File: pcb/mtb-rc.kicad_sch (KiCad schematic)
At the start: 44 parts, among them J1 MVE252-5-V, J10 MVE252-5-V, J11 MVE252-5-V, J2 MVE252-5-V, J3 MVE252-5-V, J4 MVE252-5-V, J5 MVE252-5-V, J9 MVE252-5-V, U1 VO0631T, U2 VO0631T, U3 VO0631T

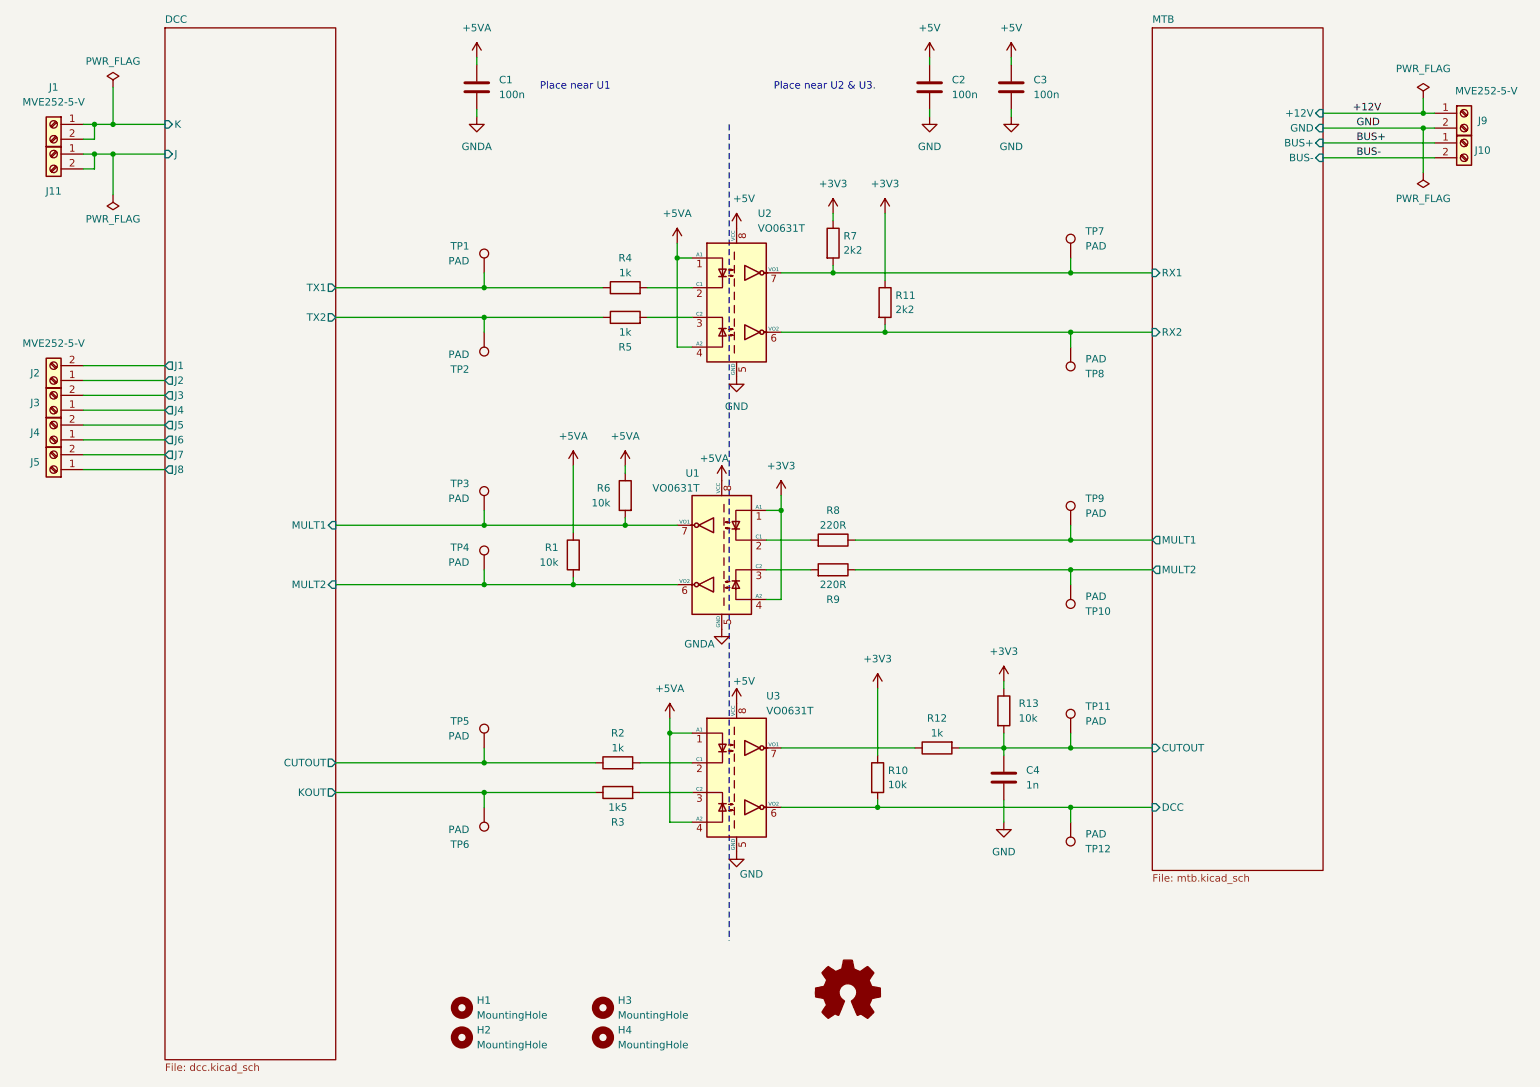
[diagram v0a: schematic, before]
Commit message: Use 2×MVE252-5-V footprint.
To avoid DRC issues in PCB.
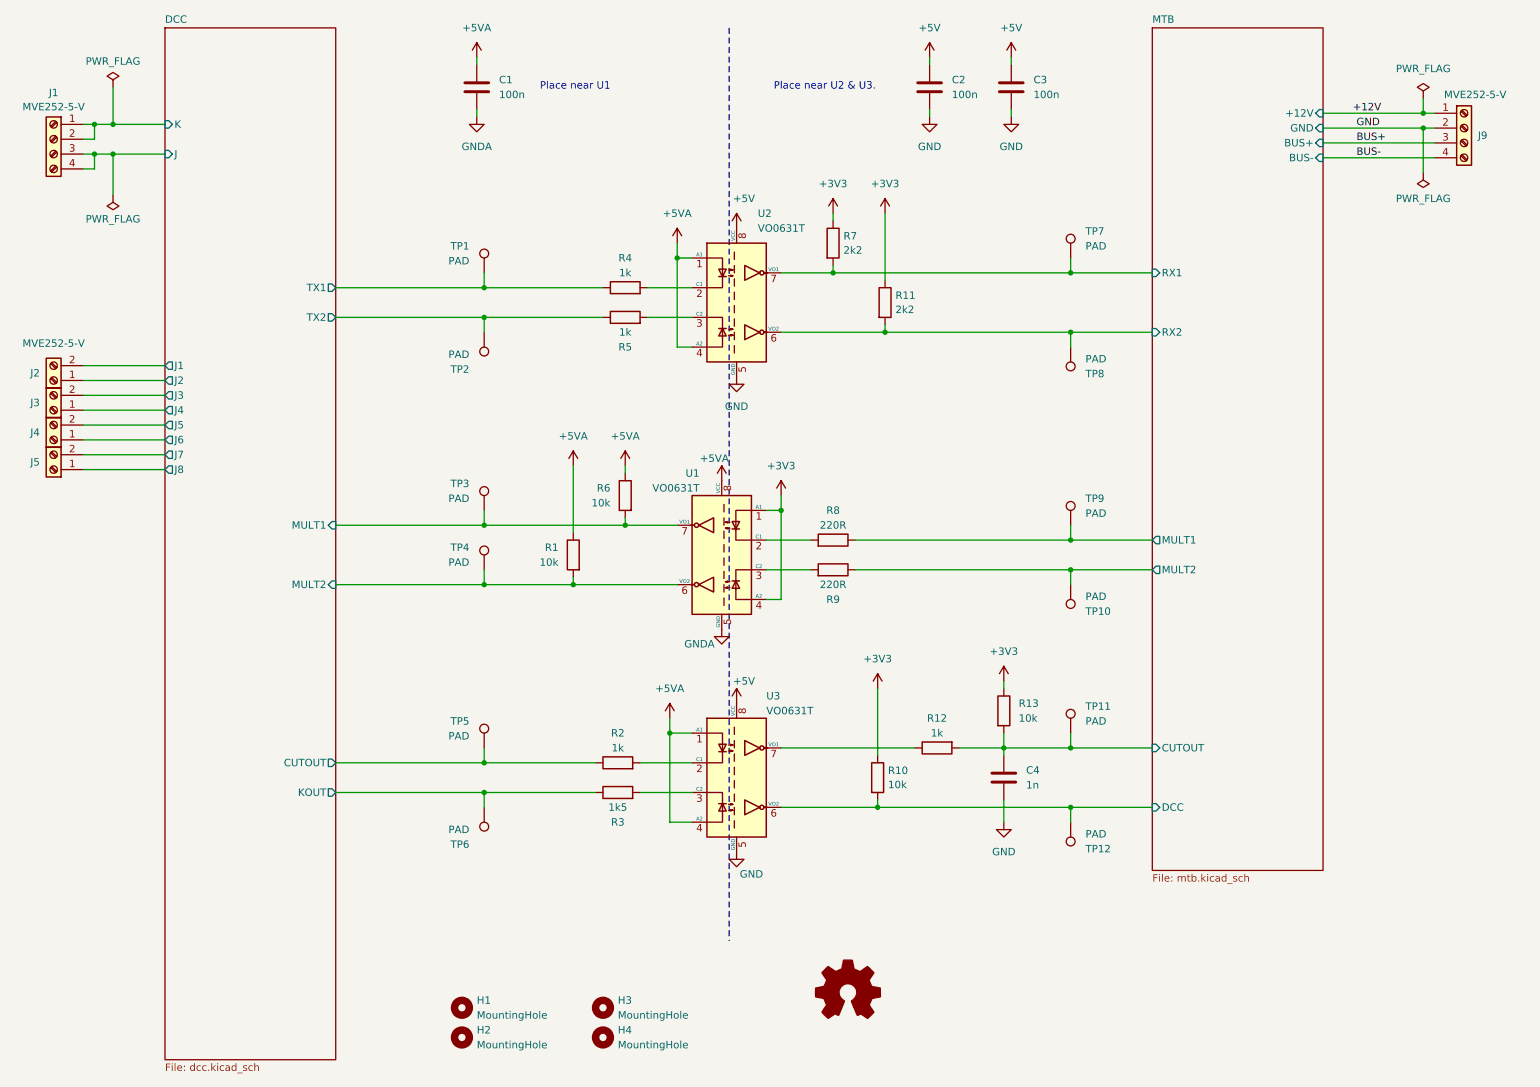
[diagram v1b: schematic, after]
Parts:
- removed J10, J11: MVE252-5-V, TerminalBlock_Euroclamp:MVE252-5-V, symbol Connector:Screw_Terminal_01x02
- J1, J9: footprint TerminalBlock_Euroclamp:MVE252-5-V -> TerminalBlock_Euroclamp:MVE252-5-V-2x; symbol Connector:Screw_Terminal_01x02 -> Connector:Screw_Terminal_01x04
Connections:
- net BUS+: now also J9.3 (Pin_3)
- net BUS-: now also J9.4 (Pin_4)
- net DCC/J: now also J1.3 (Pin_3), J1.4 (Pin_4)
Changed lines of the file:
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@@
     (stroke (width 0) (type default))
   )
-  (polyline (pts (xy 144.78 33.02) (xy 144.78 172.72))
+  (polyline (pts (xy 144.78 16.51) (xy 144.78 172.72))
     (stroke (width 0) (type dash))
   )
@@
     )
   )
-  (symbol (lib_id "Connector:Screw_Terminal_01x02") (at 29.21 33.02 0) (mirror y) (unit 1)
-    (in_bom yes) (on_board yes) (dnp no) (fields_autoplaced)
-    (property "Reference" "J1" (at 29.21 26.67 0)
-      (effects (font (size 1.27 1.27)))
-    )
-    (property "Value" "MVE252-5-V" (at 29.21 29.21 0)
-      (effects (font (size 1.27 1.27)))
-    )
-    (property "Footprint" "TerminalBlock_Euroclamp:MVE252-5-V" (at 29.21 33.02 0)
-      (effects (font (size 1.27 1.27)) hide)
-    )
-    (property "Datasheet" "~" (at 29.21 33.02 0)
-      (effects (font (size 1.27 1.27)) hide)
-    )
-    (pin "1")
-    (pin "2")
+  (symbol (lib_id "Connector:Screw_Terminal_01x04") (at 29.21 35.56 0) (mirror y) (unit 1)
+    (in_bom yes) (on_board yes) (dnp no) (fields_autoplaced)
+    (property "Reference" "J1" (at 29.21 27.6057 0)
+      (effects (font (size 1.27 1.27)))
+    )
+    (property "Value" "MVE252-5-V" (at 29.21 30.0299 0)
+      (effects (font (size 1.27 1.27)))
+    )
+    (property "Footprint" "TerminalBlock_Euroclamp:MVE252-5-V-2x" (at 29.21 35.56 0)
+      (effects (font (size 1.27 1.27)) hide)
+    )
+    (property "Datasheet" "~" (at 29.21 35.56 0)
+      (effects (font (size 1.27 1.27)) hide)
+    )
+    (pin "1")
+    (pin "2")
+    (pin "3")
+    (pin "4")
     (instances
       (project "mtb-rc"
@@
     )
   )
-  (symbol (lib_id "Connector:Screw_Terminal_01x02") (at 270.51 31.115 0) (unit 1)
-    (in_bom yes) (on_board yes) (dnp no)
-    (property "Reference" "J9" (at 273.685 32.385 0)
-      (effects (font (size 1.27 1.27)))
-    )
-    (property "Value" "MVE252-5-V" (at 274.32 27.305 0)
-      (effects (font (size 1.27 1.27)))
-    )
-    (property "Footprint" "TerminalBlock_Euroclamp:MVE252-5-V" (at 270.51 31.115 0)
-      (effects (font (size 1.27 1.27)) hide)
-    )
-    (property "Datasheet" "~" (at 270.51 31.115 0)
-      (effects (font (size 1.27 1.27)) hide)
-    )
-    (pin "1")
-    (pin "2")
+  (symbol (lib_id "Connector:Screw_Terminal_01x04") (at 270.51 33.655 0) (unit 1)
+    (in_bom yes) (on_board yes) (dnp no)
+    (property "Reference" "J9" (at 273.685 34.925 0)
+      (effects (font (size 1.27 1.27)))
+    )
+    (property "Value" "MVE252-5-V" (at 272.415 27.94 0)
+      (effects (font (size 1.27 1.27)))
+    )
+    (property "Footprint" "TerminalBlock_Euroclamp:MVE252-5-V-2x" (at 270.51 33.655 0)
+      (effects (font (size 1.27 1.27)) hide)
+    )
+    (property "Datasheet" "~" (at 270.51 33.655 0)
+      (effects (font (size 1.27 1.27)) hide)
+    )
+    (pin "1")
+    (pin "2")
+    (pin "3")
+    (pin "4")
     (instances
       (project "mtb-rc"
@@
         (path "/3e59d29f-2657-4552-9290-3c54fadfdf63"
           (reference "#FLG01") (unit 1)
-        )
-      )
-    )
-  )
-  (symbol (lib_id "Connector:Screw_Terminal_01x02") (at 29.21 38.1 0) (mirror y) (unit 1)
-    (in_bom yes) (on_board yes) (dnp no)
-    (property "Reference" "J11" (at 29.21 44.45 0)
-      (effects (font (size 1.27 1.27)))
-    )
-    (property "Value" "MVE252-5-V" (at 29.21 34.29 0)
-      (effects (font (size 1.27 1.27)) hide)
-    )
-    (property "Footprint" "TerminalBlock_Euroclamp:MVE252-5-V" (at 29.21 38.1 0)
-      (effects (font (size 1.27 1.27)) hide)
-    )
-    (property "Datasheet" "~" (at 29.21 38.1 0)
-      (effects (font (size 1.27 1.27)) hide)
-    )
-    (pin "1")
-    (pin "2")
-    (instances
-      (project "mtb-rc"
-        (path "/3e59d29f-2657-4552-9290-3c54fadfdf63"
-          (reference "J11") (unit 1)
         )
       )
@@
         )
       )
-    )
-  )
-  (symbol (lib_id "Connector:Screw_Terminal_01x02") (at 270.51 36.195 0) (unit 1)
-    (in_bom yes) (on_board yes) (dnp no)
-    (property "Reference" "J10" (at 273.685 37.465 0)
-      (effects (font (size 1.27 1.27)))
-    )
-    (property "Value" "MVE252-5-V" (at 270.51 32.385 0)
-      (effects (font (size 1.27 1.27)) hide)
-    )
-    (property "Footprint" "TerminalBlock_Euroclamp:MVE252-5-V" (at 270.51 36.195 0)
-      (effects (font (size 1.27 1.27)) hide)
-    )
-    (property "Datasheet" "~" (at 270.51 36.195 0)
-      (effects (font (size 1.27 1.27)) hide)
-    )
-    (pin "1")
-    (pin "2")
-    (instances
-      (project "mtb-rc"
-        (path "/3e59d29f-2657-4552-9290-3c54fadfdf63"
-          (reference "J10") (unit 1)
-        )
-      )

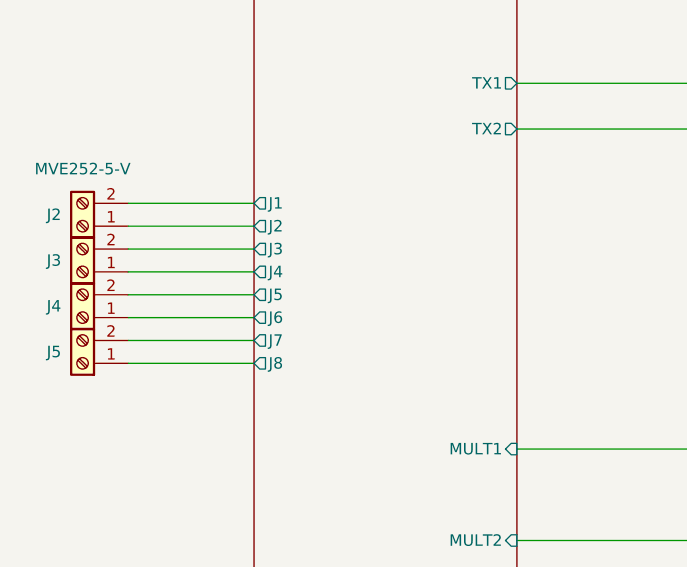
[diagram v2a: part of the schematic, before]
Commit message: J1-J8 -> J0-J7.
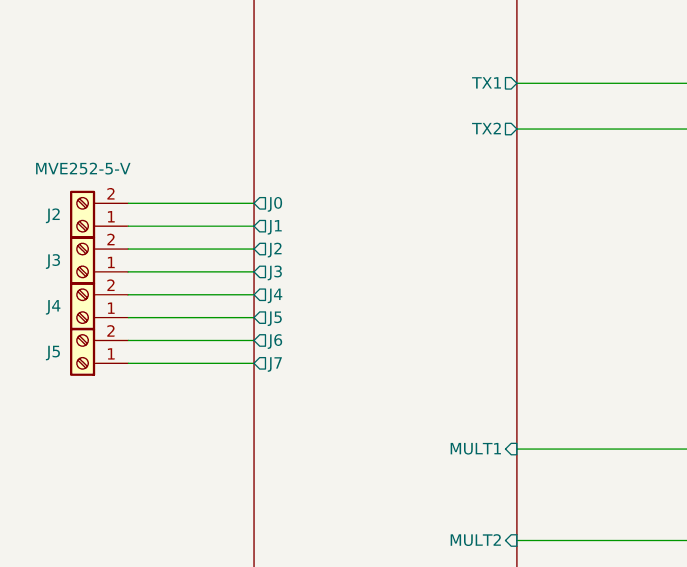
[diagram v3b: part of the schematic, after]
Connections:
- net DCC/J8 is gone; now on net DCC/J7: J5.1 (Pin_1)
- net DCC/J1: now also J2.1 (Pin_1); no longer J2.2 (Pin_2)
- net DCC/J2: now also J3.2 (Pin_2); no longer J2.1 (Pin_1)
- net DCC/J3: now also J3.1 (Pin_1); no longer J3.2 (Pin_2)
- net DCC/J4: now also J4.2 (Pin_2); no longer J3.1 (Pin_1)
- net DCC/J5: now also J4.1 (Pin_1); no longer J4.2 (Pin_2)
- net DCC/J6: now also J5.2 (Pin_2); no longer J4.1 (Pin_1)
- net DCC/J7: no longer J5.2 (Pin_2)
- new net DCC/J0: J2.2 (Pin_2)
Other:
- sheet DCC ports: added J0; removed J8
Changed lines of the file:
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@@
       (effects (font (size 1.27 1.27)) (justify left))
     )
-    (pin "J1" output (at 48.26 74.295 180)
+    (pin "J0" output (at 48.26 74.295 180)
       (effects (font (size 1.27 1.27)) (justify left))
     )
-    (pin "J2" output (at 48.26 76.835 180)
+    (pin "J1" output (at 48.26 76.835 180)
       (effects (font (size 1.27 1.27)) (justify left))
     )
-    (pin "J4" output (at 48.26 81.915 180)
+    (pin "J3" output (at 48.26 81.915 180)
       (effects (font (size 1.27 1.27)) (justify left))
     )
-    (pin "J3" output (at 48.26 79.375 180)
+    (pin "J2" output (at 48.26 79.375 180)
       (effects (font (size 1.27 1.27)) (justify left))
     )
-    (pin "J8" output (at 48.26 92.075 180)
+    (pin "J7" output (at 48.26 92.075 180)
       (effects (font (size 1.27 1.27)) (justify left))
     )
-    (pin "J7" output (at 48.26 89.535 180)
+    (pin "J6" output (at 48.26 89.535 180)
       (effects (font (size 1.27 1.27)) (justify left))
     )
@@
       (effects (font (size 1.27 1.27)) (justify right))
     )
-    (pin "J5" output (at 48.26 84.455 180)
+    (pin "J4" output (at 48.26 84.455 180)
       (effects (font (size 1.27 1.27)) (justify left))
     )
-    (pin "J6" output (at 48.26 86.995 180)
+    (pin "J5" output (at 48.26 86.995 180)
       (effects (font (size 1.27 1.27)) (justify left))
     )

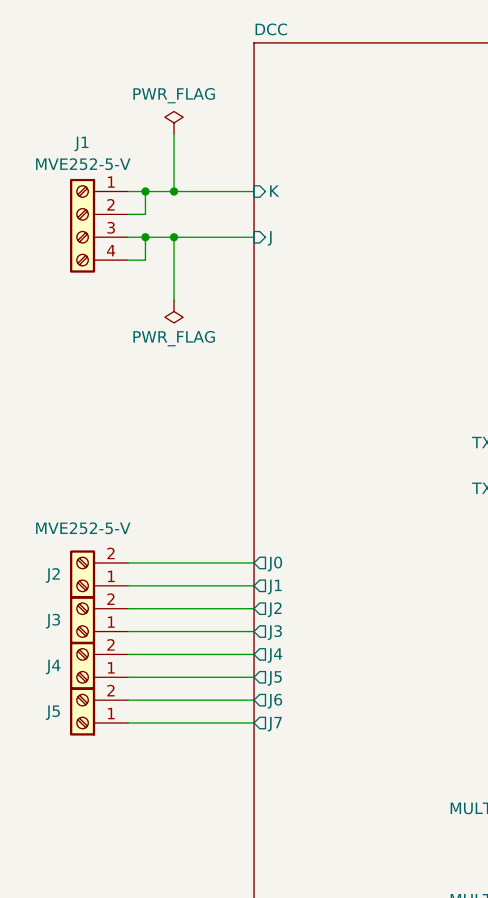
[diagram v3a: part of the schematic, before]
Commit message: Use 4×MVE252-5-V footprint.
To avoid DRC issues in schematics.
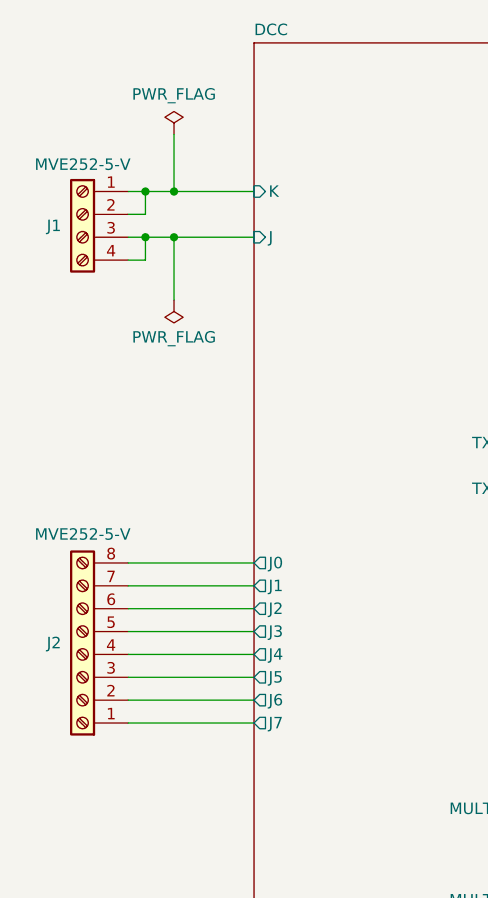
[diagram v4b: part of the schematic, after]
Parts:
- removed J3, J4, J5: MVE252-5-V, TerminalBlock_Euroclamp:MVE252-5-V, symbol Connector:Screw_Terminal_01x02
- J2: footprint TerminalBlock_Euroclamp:MVE252-5-V -> TerminalBlock_Euroclamp:MVE252-5-V-4x; symbol Connector:Screw_Terminal_01x02 -> Connector:Screw_Terminal_01x08
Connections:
- net DCC/J0: now also J2.8 (Pin_8); no longer J2.2 (Pin_2)
- net DCC/J1: now also J2.7 (Pin_7); no longer J2.1 (Pin_1)
- net DCC/J2: now also J2.6 (Pin_6)
- net DCC/J3: now also J2.5 (Pin_5)
- net DCC/J4: now also J2.4 (Pin_4)
- net DCC/J5: now also J2.3 (Pin_3)
- net DCC/J6: now also J2.2 (Pin_2)
- net DCC/J7: now also J2.1 (Pin_1)
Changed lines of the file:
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@@
-    )
-  )
-  (symbol (lib_id "Connector:Screw_Terminal_01x02") (at 29.21 86.995 180) (unit 1)
-    (in_bom yes) (on_board yes) (dnp no)
-    (property "Reference" "J4" (at 26.035 85.725 0)
-      (effects (font (size 1.27 1.27)))
-    )
-    (property "Value" "MVE252-5-V" (at 29.21 90.805 0)
-      (effects (font (size 1.27 1.27)) hide)
-    )
-    (property "Footprint" "TerminalBlock_Euroclamp:MVE252-5-V" (at 29.21 86.995 0)
-      (effects (font (size 1.27 1.27)) hide)
-    )
-    (property "Datasheet" "~" (at 29.21 86.995 0)
-      (effects (font (size 1.27 1.27)) hide)
-    )
-    (pin "1")
-    (pin "2")
-    (instances
-      (project "mtb-rc"
-        (path "/3e59d29f-2657-4552-9290-3c54fadfdf63"
-          (reference "J4") (unit 1)
-        )
-      )
     )
   )
@@
   )
   (symbol (lib_id "Connector:Screw_Terminal_01x04") (at 29.21 35.56 0) (mirror y) (unit 1)
-    (in_bom yes) (on_board yes) (dnp no) (fields_autoplaced)
-    (property "Reference" "J1" (at 29.21 27.6057 0)
+    (in_bom yes) (on_board yes) (dnp no)
+    (property "Reference" "J1" (at 26.035 36.83 0)
       (effects (font (size 1.27 1.27)))
     )
@@
         (path "/3e59d29f-2657-4552-9290-3c54fadfdf63"
           (reference "C1") (unit 1)
-        )
-      )
-    )
-  )
-  (symbol (lib_id "Connector:Screw_Terminal_01x02") (at 29.21 81.915 180) (unit 1)
-    (in_bom yes) (on_board yes) (dnp no)
-    (property "Reference" "J3" (at 26.035 80.645 0)
-      (effects (font (size 1.27 1.27)))
-    )
-    (property "Value" "MVE252-5-V" (at 29.21 85.725 0)
-      (effects (font (size 1.27 1.27)) hide)
-    )
-    (property "Footprint" "TerminalBlock_Euroclamp:MVE252-5-V" (at 29.21 81.915 0)
-      (effects (font (size 1.27 1.27)) hide)
-    )
-    (property "Datasheet" "~" (at 29.21 81.915 0)
-      (effects (font (size 1.27 1.27)) hide)
-    )
-    (pin "1")
-    (pin "2")
-    (instances
-      (project "mtb-rc"
-        (path "/3e59d29f-2657-4552-9290-3c54fadfdf63"
-          (reference "J3") (unit 1)
         )
       )
@@
     )
   )
-  (symbol (lib_id "Connector:Screw_Terminal_01x02") (at 29.21 92.075 180) (unit 1)
-    (in_bom yes) (on_board yes) (dnp no)
-    (property "Reference" "J5" (at 26.035 90.805 0)
-      (effects (font (size 1.27 1.27)))
-    )
-    (property "Value" "MVE252-5-V" (at 29.21 95.885 0)
-      (effects (font (size 1.27 1.27)) hide)
-    )
-    (property "Footprint" "TerminalBlock_Euroclamp:MVE252-5-V" (at 29.21 92.075 0)
-      (effects (font (size 1.27 1.27)) hide)
-    )
-    (property "Datasheet" "~" (at 29.21 92.075 0)
-      (effects (font (size 1.27 1.27)) hide)
-    )
-    (pin "1")
-    (pin "2")
-    (instances
-      (project "mtb-rc"
-        (path "/3e59d29f-2657-4552-9290-3c54fadfdf63"
-          (reference "J5") (unit 1)
-        )
-      )
-    )
-  )
   (symbol (lib_id "Device:R") (at 162.56 53.34 0) (unit 1)
     (in_bom yes) (on_board yes) (dnp no) (fields_autoplaced)
@@
     )
   )
-  (symbol (lib_id "Connector:Screw_Terminal_01x02") (at 29.21 76.835 180) (unit 1)
-    (in_bom yes) (on_board yes) (dnp no)
-    (property "Reference" "J2" (at 26.035 75.565 0)
-      (effects (font (size 1.27 1.27)))
-    )
-    (property "Value" "MVE252-5-V" (at 29.21 70.485 0)
-      (effects (font (size 1.27 1.27)))
-    )
-    (property "Footprint" "TerminalBlock_Euroclamp:MVE252-5-V" (at 29.21 76.835 0)
-      (effects (font (size 1.27 1.27)) hide)
-    )
-    (property "Datasheet" "~" (at 29.21 76.835 0)
-      (effects (font (size 1.27 1.27)) hide)
-    )
-    (pin "1")
-    (pin "2")
-    (instances
-      (project "mtb-rc"
+  (symbol (lib_id "Connector:Screw_Terminal_01x08") (at 29.21 84.455 180) (unit 1)
+    (in_bom yes) (on_board yes) (dnp no)
+    (property "Reference" "J2" (at 26.035 83.185 0)
+      (effects (font (size 1.27 1.27)))
+    )
+    (property "Value" "MVE252-5-V" (at 29.21 71.12 0)
+      (effects (font (size 1.27 1.27)))
+    )
+    (property "Footprint" "TerminalBlock_Euroclamp:MVE252-5-V-4x" (at 29.21 84.455 0)
+      (effects (font (size 1.27 1.27)) hide)
+    )
+    (property "Datasheet" "~" (at 29.21 84.455 0)
+      (effects (font (size 1.27 1.27)) hide)
+    )
+    (pin "1")
+    (pin "2")
+    (pin "3")
+    (pin "4")
+    (pin "5")
+    (pin "6")
+    (pin "7")
+    (pin "8")
+    (instances
+      (project "mtb-rc"
